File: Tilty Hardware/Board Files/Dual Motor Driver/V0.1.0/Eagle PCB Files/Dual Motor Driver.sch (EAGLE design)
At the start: 25 parts, among them U1 ATMEGA32U4TQFP, U2 L298_BRIDGE_DRIVER

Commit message: Lots of work on dual motor driver
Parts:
- removed C2: 0.1uF, resistor:C-USC0603
- removed JP10: (no value), SparkFun-Connectors:M04SMD2
- removed JP11, JP9: M11PTH, SparkFun-Connectors:M11PTH
- added C1, C7: 1uF, resistor:C-USC0603
- added C3, C5, C6: 0.1uF, resistor:C-USC0603
- added F1: PTCSMD, SparkFun-PowerIC:PTCSMD
- added J1: AVR_SPI_PRG_6PTH, SparkFun-Connectors:AVR_SPI_PRG_6PTH
- added R1, R2: 10K, resistor:R-US_R0603
- added RN1: (no value), resistor-dil:4R-N0603-ARV
- added SJ1: SOLDERJUMPERNC, SparkFun-Passives:SOLDERJUMPERNC
- added U3: PCA9306, My Parts:PCA9306
- added U4: TLV71333PDBVR, SparkFun-PowerIC:ADP160
- added U5: VOLTAGE-REGULATOR, My Parts:VOLTAGE-REGULATOR
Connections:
- removed net VUSB: JP7.VBUS, U1.VBUS
- new net +3V3: C3.1, U3.VREF1, U4.VOUT
- new net L-SCL: JP4.7, U3.SCL1
- new net L-SDA: JP4.8, U3.SDA1
- new net MISO: J1.1, U1.PB3(MISO)
- new net MOSI: J1.4, U1.PB2(MOSI)
- new net N$1: RN1D.2, U1.D+
- new net N$2: RN1A.2, U1.D-
- new net N$3: R2.1, U3.EN
- new net N$4: F1.2, JP7.VBUS
- new net N$5: JP2.2, SJ1.1
- new net RESET: J1.5, R1.1, U1.!RESET
- new net SCK: J1.3, U1.PB1(SCK)
- net +24V: now also C7.1, JP8.4, SJ1.2, U5.VIN
- net +5V: now also C1.1, C5.1, C6.1, F1.1, J1.2, R1.2, R2.2, U1.UCAP, U1.VBUS, U3.VREF2, U4.EN, U4.VIN, U5.VOUT; no longer C2.1
- net GND: now also C3.2, C5.2, C6.2, C7.2, J1.6, JP8.3, U2.GND@10, U3.GND, U4.GND, U5.GND; no longer C2.2, U2.GND@20, U2.SENSE_A, U2.SENSE_B
- net H-SCL: now also U3.SCL2; no longer JP4.7
- net H-SDA: now also U3.SDA2; no longer JP4.8
- net M1A: now also JP8.6
- net M1B: now also JP8.5
- net M2A: now also JP5.5, JP8.2
- net M2B: now also JP5.6, JP8.1
- net UGND: now also C1.2
- net USB_D+: now also RN1D.1; no longer U1.D+
- net USB_D-: now also RN1A.1; no longer U1.D-
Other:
- note added: "Not used"
- moved on the sheet: JP1, JP2, JP3, JP4, JP5, JP6, JP8, Z1, Z2

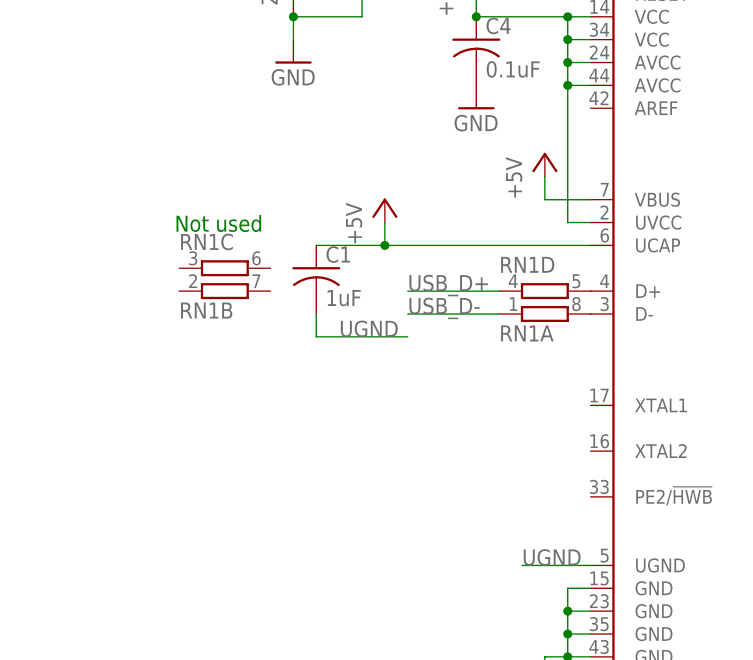
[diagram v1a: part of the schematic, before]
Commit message: Updated dual motor driver and Tilty Duo/Quad PCBs, added a copuple experimental arduino programs
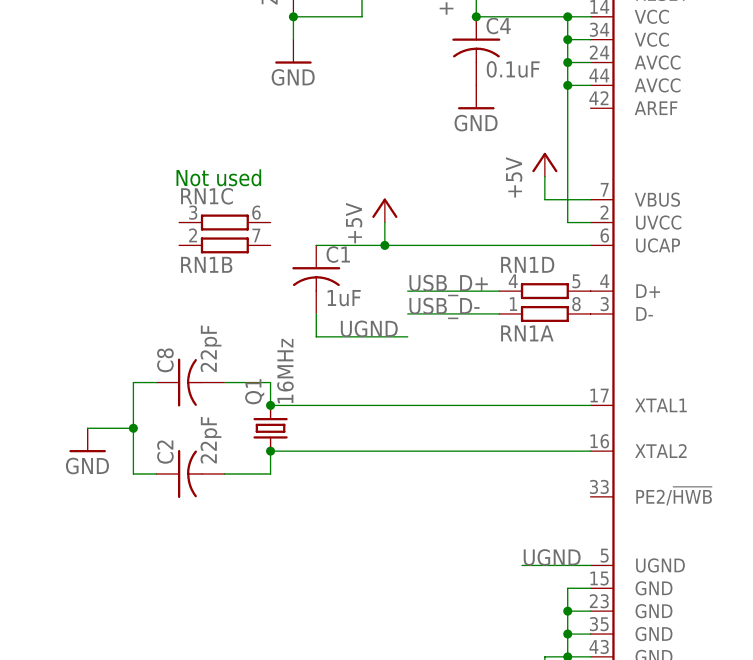
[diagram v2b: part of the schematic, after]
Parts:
- added C2, C8: 22pF, resistor:C-USC0603
- added Q1: 16MHz, crystal:CRYSTALCTS406
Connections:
- new net N$6: C8.2, Q1.2, U1.XTAL1
- new net N$7: C2.2, Q1.1, U1.XTAL2
- net GND: now also C2.1, C8.1
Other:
- moved on the sheet: RN1B, RN1C
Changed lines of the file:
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@@
 <grid distance="0.1" unitdist="inch" unit="inch" style="lines" multiple="1" display="no" altdistance="0.01" altunitdist="inch" altunit="inch"/>
 <layers>
-<layer number="1" name="Top" color="4" fill="1" visible="no" active="no"/>
-<layer number="16" name="Bottom" color="1" fill="1" visible="no" active="no"/>
-<layer number="17" name="Pads" color="2" fill="1" visible="no" active="no"/>
-<layer number="18" name="Vias" color="2" fill="1" visible="no" active="no"/>
-<layer number="19" name="Unrouted" color="6" fill="1" visible="no" active="no"/>
-<layer number="20" name="Dimension" color="15" fill="1" visible="no" active="no"/>
-<layer number="21" name="tPlace" color="7" fill="1" visible="no" active="no"/>
-<layer number="22" name="bPlace" color="7" fill="1" visible="no" active="no"/>
-<layer number="23" name="tOrigins" color="15" fill="1" visible="no" active="no"/>
-<layer number="24" name="bOrigins" color="15" fill="1" visible="no" active="no"/>
-<layer number="25" name="tNames" color="7" fill="1" visible="no" active="no"/>
-<layer number="26" name="bNames" color="7" fill="1" visible="no" active="no"/>
-<layer number="27" name="tValues" color="7" fill="1" visible="no" active="no"/>
-<layer number="28" name="bValues" color="7" fill="1" visible="no" active="no"/>
+<layer number="1" name="Top" color="4" fill="1" visible="yes" active="no"/>
+<layer number="16" name="Bottom" color="1" fill="1" visible="yes" active="no"/>
+<layer number="17" name="Pads" color="2" fill="1" visible="yes" active="no"/>
+<layer number="18" name="Vias" color="2" fill="1" visible="yes" active="no"/>
+<layer number="19" name="Unrouted" color="6" fill="1" visible="yes" active="no"/>
+<layer number="20" name="Dimension" color="15" fill="1" visible="yes" active="no"/>
+<layer number="21" name="tPlace" color="7" fill="1" visible="yes" active="no"/>
+<layer number="22" name="bPlace" color="7" fill="1" visible="yes" active="no"/>
+<layer number="23" name="tOrigins" color="15" fill="1" visible="yes" active="no"/>
+<layer number="24" name="bOrigins" color="15" fill="1" visible="yes" active="no"/>
+<layer number="25" name="tNames" color="7" fill="1" visible="yes" active="no"/>
+<layer number="26" name="bNames" color="7" fill="1" visible="yes" active="no"/>
+<layer number="27" name="tValues" color="7" fill="1" visible="yes" active="no"/>
+<layer number="28" name="bValues" color="7" fill="1" visible="yes" active="no"/>
 <layer number="29" name="tStop" color="7" fill="3" visible="no" active="no"/>
 <layer number="30" name="bStop" color="7" fill="6" visible="no" active="no"/>
@@
 <layer number="35" name="tGlue" color="7" fill="4" visible="no" active="no"/>
 <layer number="36" name="bGlue" color="7" fill="5" visible="no" active="no"/>
-<layer number="37" name="tTest" color="7" fill="1" visible="no" active="no"/>
-<layer number="38" name="bTest" color="7" fill="1" visible="no" active="no"/>
+<layer number="37" name="tTest" color="7" fill="1" visible="yes" active="no"/>
+<layer number="38" name="bTest" color="7" fill="1" visible="yes" active="no"/>
 <layer number="39" name="tKeepout" color="4" fill="11" visible="no" active="no"/>
 <layer number="40" name="bKeepout" color="1" fill="11" visible="no" active="no"/>
@@
 <layer number="44" name="Drills" color="7" fill="1" visible="no" active="no"/>
 <layer number="45" name="Holes" color="7" fill="1" visible="no" active="no"/>
-<layer number="46" name="Milling" color="3" fill="1" visible="no" active="no"/>
-<layer number="47" name="Measures" color="7" fill="1" visible="no" active="no"/>
-<layer number="48" name="Document" color="7" fill="1" visible="no" active="no"/>
-<layer number="49" name="Reference" color="7" fill="1" visible="no" active="no"/>
-<layer number="50" name="dxf" color="7" fill="1" visible="no" active="no"/>
-<layer number="51" name="tDocu" color="7" fill="1" visible="no" active="no"/>
-<layer number="52" name="bDocu" color="7" fill="1" visible="no" active="no"/>
-<layer number="53" name="tGND_GNDA" color="7" fill="9" visible="no" active="no"/>
-<layer number="54" name="bGND_GNDA" color="1" fill="9" visible="no" active="no"/>
-<layer number="56" name="wert" color="7" fill="1" visible="no" active="no"/>
+<layer number="46" name="Milling" color="3" fill="1" visible="yes" active="no"/>
+<layer number="47" name="Measures" color="7" fill="1" visible="yes" active="no"/>
+<layer number="48" name="Document" color="7" fill="1" visible="yes" active="no"/>
+<layer number="49" name="Reference" color="7" fill="1" visible="yes" active="no"/>
+<layer number="50" name="dxf" color="7" fill="1" visible="yes" active="no"/>
+<layer number="51" name="tDocu" color="7" fill="1" visible="yes" active="no"/>
+<layer number="52" name="bDocu" color="7" fill="1" visible="yes" active="no"/>
+<layer number="53" name="tGND_GNDA" color="7" fill="9" visible="yes" active="no"/>
+<layer number="54" name="bGND_GNDA" color="1" fill="9" visible="yes" active="no"/>
+<layer number="56" name="wert" color="7" fill="1" visible="yes" active="no"/>
 <layer number="91" name="Nets" color="2" fill="1" visible="yes" active="yes"/>
 <layer number="92" name="Busses" color="1" fill="1" visible="yes" active="yes"/>
@@
 <part name="P+17" library="supply1" deviceset="+24V" device=""/>
 <part name="SJ1" library="SparkFun-Passives" deviceset="SOLDERJUMPER" device="NC"/>
+<part name="Q1" library="crystal" deviceset="CRYSTAL" device="CTS406" value="16MHz">
+<attribute name="PART#" value="406C35D16M00000"/>
+</part>
+<part name="C2" library="resistor" deviceset="C-US" device="C0603" value="22pF"/>
+<part name="C8" library="resistor" deviceset="C-US" device="C0603" value="22pF"/>
+<part name="GND12" library="supply1" deviceset="GND" device=""/>
 </parts>
 <sheets>
 <sheet>
 <plain>
-<text x="17.272" y="54.864" size="1.778" layer="91">Not used</text>
+<text x="17.272" y="59.944" size="1.778" layer="91">Not used</text>
 </plain>
 <instances>
@@
 <instance part="P+6" gate="1" x="58.42" y="96.52"/>
 <instance part="RN1" gate="A" x="58.42" y="45.72"/>
-<instance part="RN1" gate="B" x="22.86" y="48.26"/>
-<instance part="RN1" gate="C" x="22.86" y="50.8" smashed="yes">
-<attribute name="VALUE" x="25.4" y="47.752" size="1.778" layer="96"/>
-<attribute name="NAME" x="17.78" y="52.832" size="1.778" layer="95"/>
+<instance part="RN1" gate="B" x="22.86" y="53.34"/>
+<instance part="RN1" gate="C" x="22.86" y="55.88" smashed="yes">
+<attribute name="VALUE" x="25.4" y="52.832" size="1.778" layer="96"/>
+<attribute name="NAME" x="17.78" y="57.912" size="1.778" layer="95"/>
 </instance>
 <instance part="RN1" gate="D" x="58.42" y="48.26" smashed="yes">
@@
 <attribute name="NAME" x="254" y="86.36" size="1.778" layer="95"/>
 </instance>
+<instance part="Q1" gate="G$1" x="27.94" y="33.02" rot="R90">
+<attribute name="PART#" x="27.94" y="33.02" size="1.778" layer="96" rot="R90" display="off"/>
+</instance>
+<instance part="C2" gate="G$1" x="17.78" y="27.94" rot="R90"/>
+<instance part="C8" gate="G$1" x="17.78" y="38.1" rot="R90"/>
+<instance part="GND12" gate="1" x="7.62" y="30.48"/>
 </instances>
 <busses>
@@
 <wire x1="60.96" y1="121.92" x2="60.96" y2="124.46" width="0.1524" layer="91"/>
 <pinref part="GND11" gate="1" pin="GND"/>
+</segment>
+<segment>
+<pinref part="C2" gate="G$1" pin="1"/>
+<wire x1="15.24" y1="27.94" x2="12.7" y2="27.94" width="0.1524" layer="91"/>
+<pinref part="GND12" gate="1" pin="GND"/>
+<wire x1="12.7" y1="27.94" x2="12.7" y2="33.02" width="0.1524" layer="91"/>
+<wire x1="12.7" y1="33.02" x2="7.62" y2="33.02" width="0.1524" layer="91"/>
+<pinref part="C8" gate="G$1" pin="1"/>
+<wire x1="15.24" y1="38.1" x2="12.7" y2="38.1" width="0.1524" layer="91"/>
+<wire x1="12.7" y1="38.1" x2="12.7" y2="33.02" width="0.1524" layer="91"/>
+<junction x="12.7" y="33.02"/>
 </segment>
 </net>
@@
 </segment>
 </net>
+<net name="N$6" class="0">
+<segment>
+<pinref part="Q1" gate="G$1" pin="2"/>
+<pinref part="C8" gate="G$1" pin="2"/>
+<wire x1="27.94" y1="35.56" x2="27.94" y2="38.1" width="0.1524" layer="91"/>
+<wire x1="27.94" y1="38.1" x2="22.86" y2="38.1" width="0.1524" layer="91"/>
+<pinref part="U1" gate="G$1" pin="XTAL1"/>
+<wire x1="27.94" y1="35.56" x2="63.5" y2="35.56" width="0.1524" layer="91"/>
+<junction x="27.94" y="35.56"/>
+</segment>
+</net>
+<net name="N$7" class="0">
+<segment>
+<pinref part="Q1" gate="G$1" pin="1"/>
+<pinref part="C2" gate="G$1" pin="2"/>
+<wire x1="27.94" y1="30.48" x2="27.94" y2="27.94" width="0.1524" layer="91"/>
+<wire x1="27.94" y1="27.94" x2="22.86" y2="27.94" width="0.1524" layer="91"/>
+<pinref part="U1" gate="G$1" pin="XTAL2"/>
+<wire x1="27.94" y1="30.48" x2="63.5" y2="30.48" width="0.1524" layer="91"/>
+<junction x="27.94" y="30.48"/>
+</segment>
+</net>

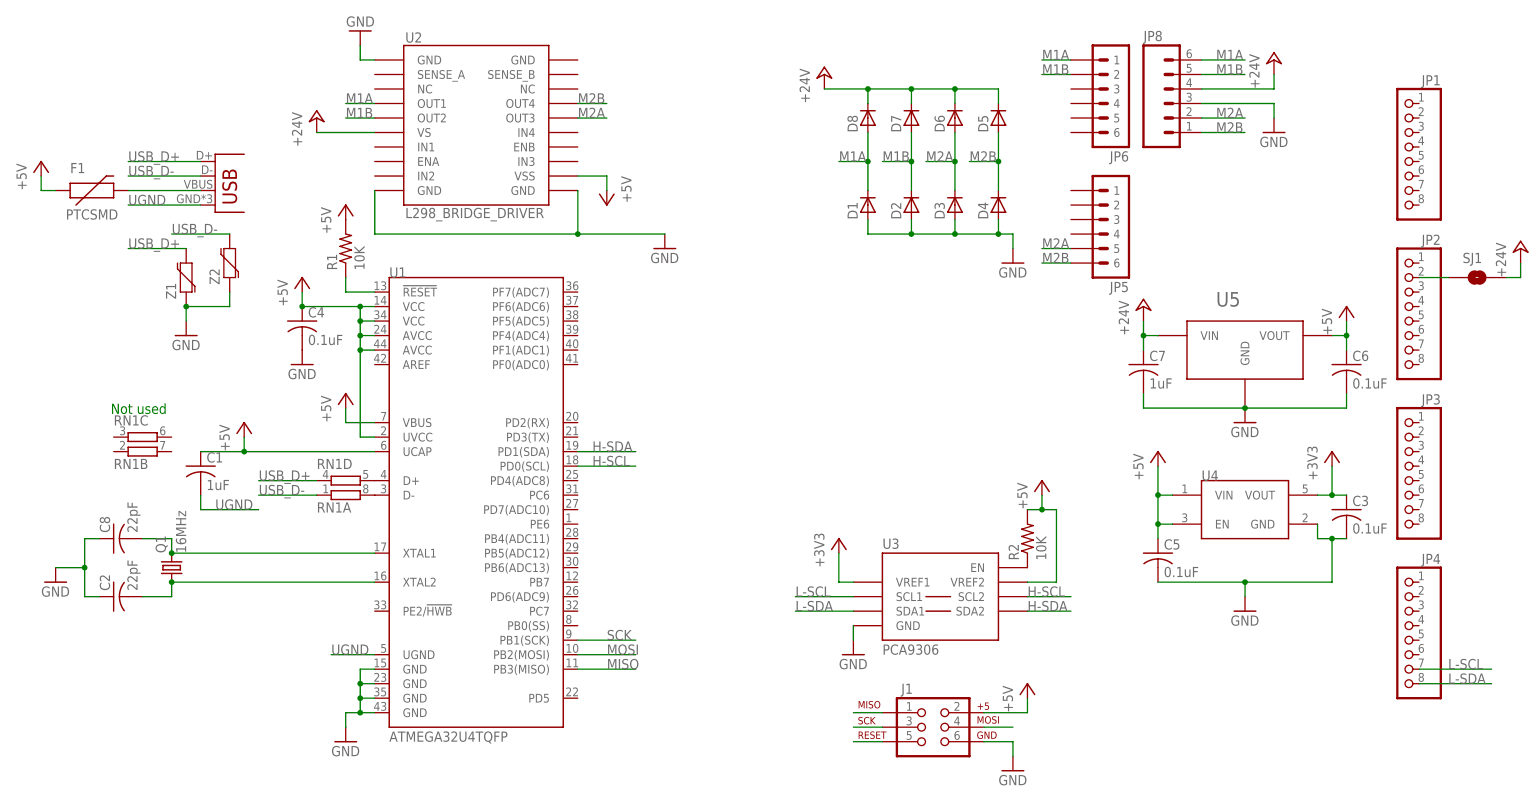
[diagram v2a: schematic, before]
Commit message: Dual motor driver add-on design
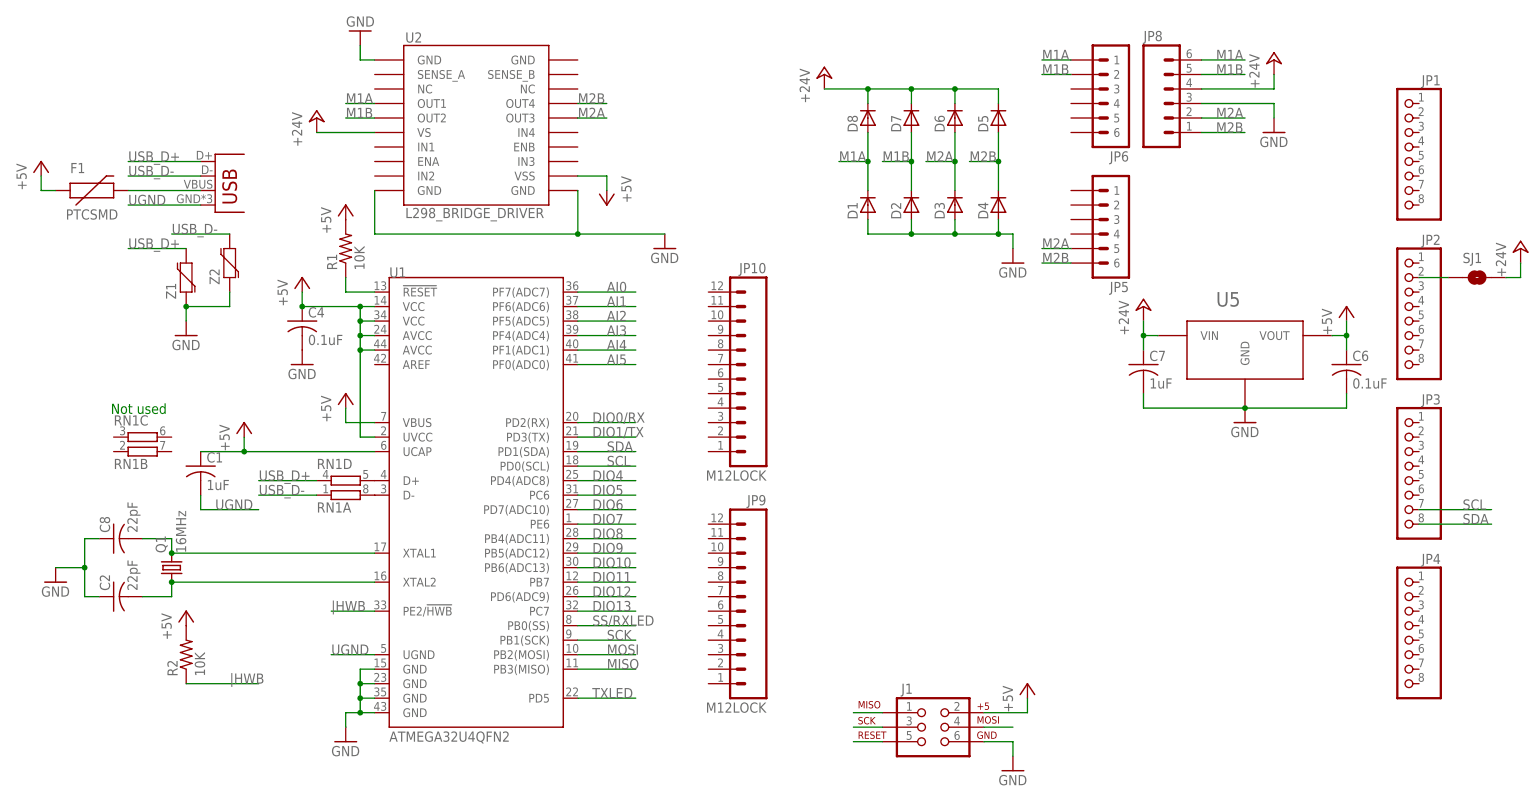
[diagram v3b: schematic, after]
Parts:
- removed C3, C5: 0.1uF, resistor:C-USC0603
- removed U3: PCA9306, My Parts:PCA9306
- removed U4: TLV71333PDBVR, SparkFun-PowerIC:ADP160
- added JP10, JP9: M12LOCK, SparkFun-Connectors:M12LOCK
- U1: value ATMEGA32U4TQFP -> ATMEGA32U4QFN2; device SparkFun-DigitalIC:ATMEGA32U4TQFP -> SparkFun-DigitalIC:ATMEGA32U4QFN2
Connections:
- removed net +3V3: C3.1, U3.VREF1, U4.VOUT
- removed net H-SCL: U1.PD0(SCL), U3.SCL2
- removed net H-SDA: U1.PD1(SDA), U3.SDA2
- removed net L-SCL: JP4.7, U3.SCL1
- removed net L-SDA: JP4.8, U3.SDA1
- removed net N$3: R2.1, U3.EN
- new net AI0: U1.PF7(ADC7)
- new net AI1: U1.PF6(ADC6)
- new net AI2: U1.PF5(ADC5)
- new net AI3: U1.PF4(ADC4)
- new net AI4: U1.PF1(ADC1)
- new net AI5: U1.PF0(ADC0)
- new net DIO0/RX: U1.PD2(RX)
- new net DIO1/TX: U1.PD3(TX)
- new net DIO10: U1.PB6(ADC13)
- new net DIO11: U1.PB7
- new net DIO12: U1.PD6(ADC9)
- new net DIO13: U1.PC7
- new net DIO4: U1.PD4(ADC8)
- new net DIO5: U1.PC6
- new net DIO6: U1.PD7(ADC10)
- new net DIO7: U1.PE6
- new net DIO8: U1.PB4(ADC11)
- new net DIO9: U1.PB5(ADC12)
- new net SCL: JP3.7, U1.PD0(SCL)
- new net SDA: JP3.8, U1.PD1(SDA)
- new net SS/RXLED: U1.PB0(SS)
- new net TXLED: U1.PD5
- new net |HWB: R2.1, U1.PE2/!HWB
- net +5V: no longer C5.1, U3.VREF2, U4.EN, U4.VIN
- net GND: no longer C3.2, C5.2, U3.GND, U4.GND
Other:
- moved on the sheet: R2

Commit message: Dual motor driver pcb work
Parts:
- removed JP10, JP9: M12LOCK, SparkFun-Connectors:M12LOCK
- added S1: SWITCH-MOMENTARY-2SMD, SparkFun-Electromechanical:SWITCH-MOMENTARY-2SMD
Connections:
- removed net DIO0/RX: U1.PD2(RX)
- removed net DIO1/TX: U1.PD3(TX)
- removed net DIO10: U1.PB6(ADC13)
- removed net DIO12: U1.PD6(ADC9)
- removed net DIO4: U1.PD4(ADC8)
- removed net DIO5: U1.PC6
- removed net DIO6: U1.PD7(ADC10)
- removed net DIO7: U1.PE6
- removed net DIO8: U1.PB4(ADC11)
- removed net DIO9: U1.PB5(ADC12)
- new net ENC1A: JP6.3, U1.PE6
- new net ENC1B: JP6.4, U1.PD2(RX)
- new net ENC2A: JP5.4, U1.PD6(ADC9)
- new net ENC2B: JP5.3, U1.PD3(TX)
- new net M1+: U1.PD4(ADC8), U2.IN1
- new net M1-: U1.PB4(ADC11), U2.IN2
- new net M2+: U1.PC6, U2.IN3
- new net M2-: U1.PD7(ADC10), U2.IN4
- new net PWM1: U1.PB5(ADC12), U2.ENA
- new net PWM2: U1.PB6(ADC13), U2.ENB
- net +5V: now also JP5.1, JP6.6
- net GND: now also JP5.2, JP6.5, S1.1
- net |HWB: now also S1.2
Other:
- note added: "Change to a non- Sparkfun button"
- moved on the sheet: D1, D2, D3, D4, D5, D6, D7, D8
